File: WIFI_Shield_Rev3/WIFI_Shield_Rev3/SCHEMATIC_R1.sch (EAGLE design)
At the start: 32 parts, among them M1 NUCLEO-L452RE, U1 APDS-9306-065, U5 ESP32-C3-WROOM-02-N4

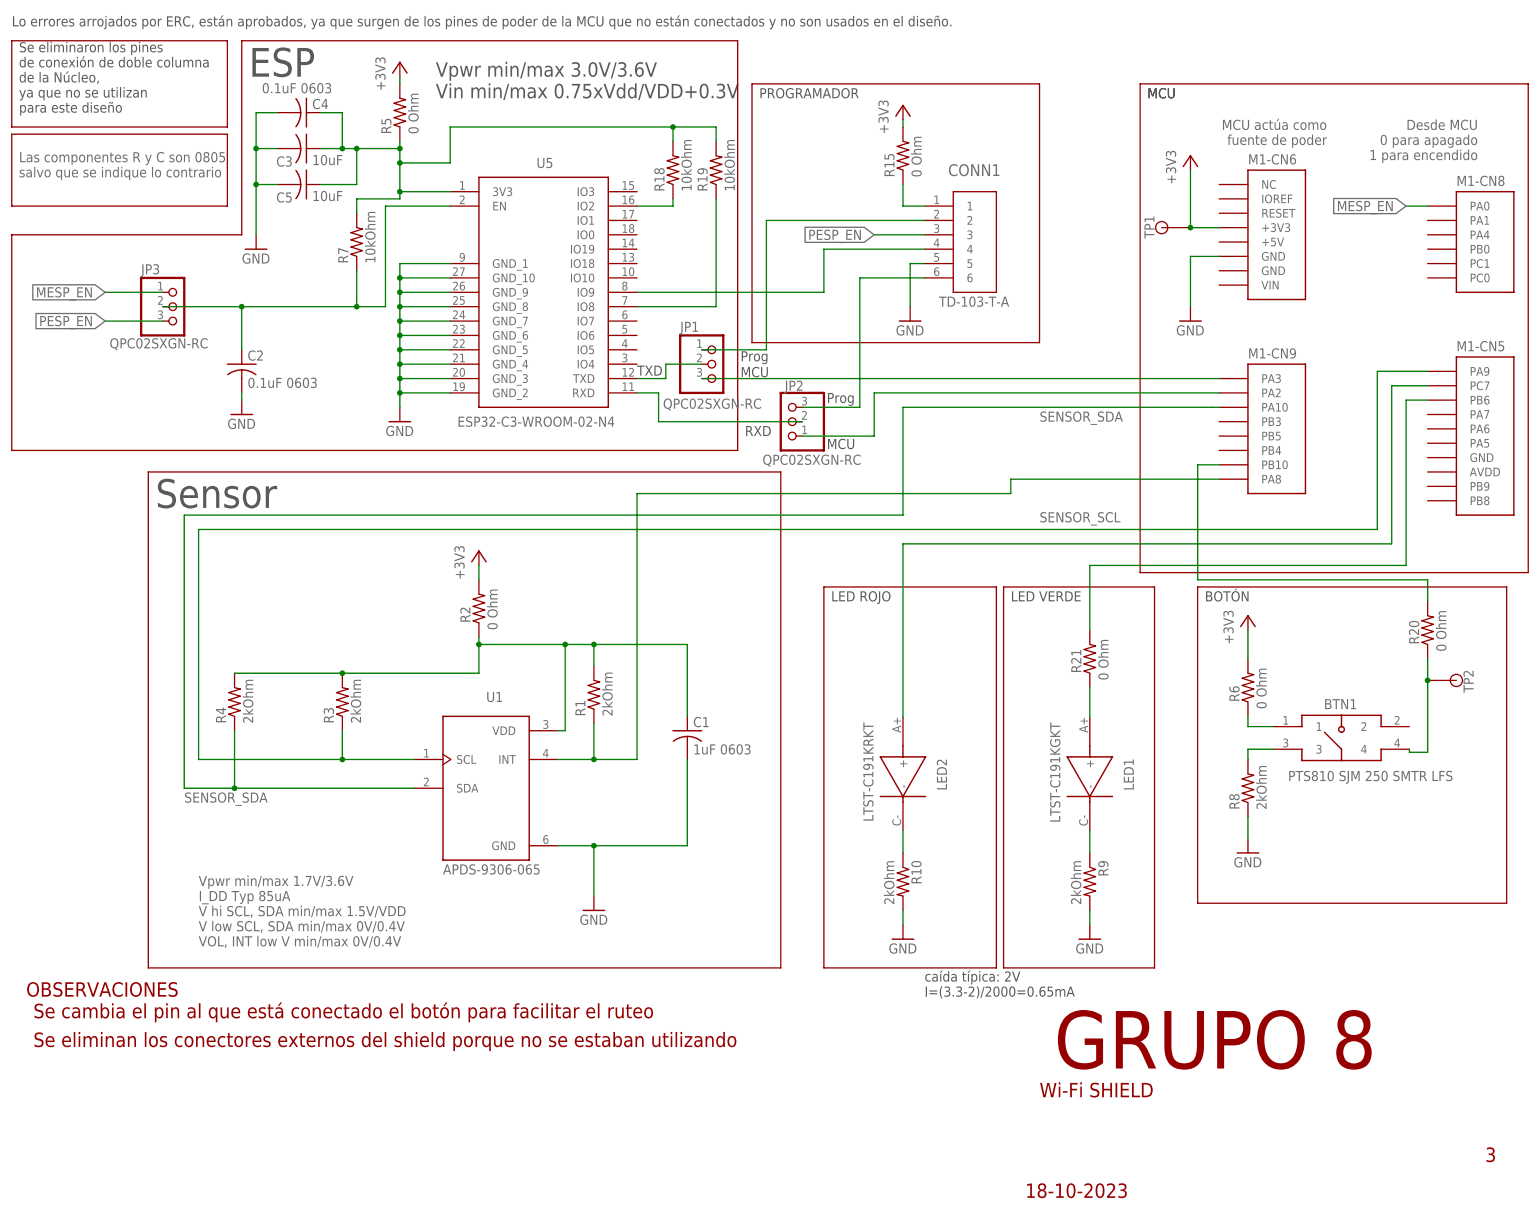
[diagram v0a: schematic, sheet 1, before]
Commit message: Arreglados los jumpers que no aparecían en el BOM. Agregados comentarios adicionales
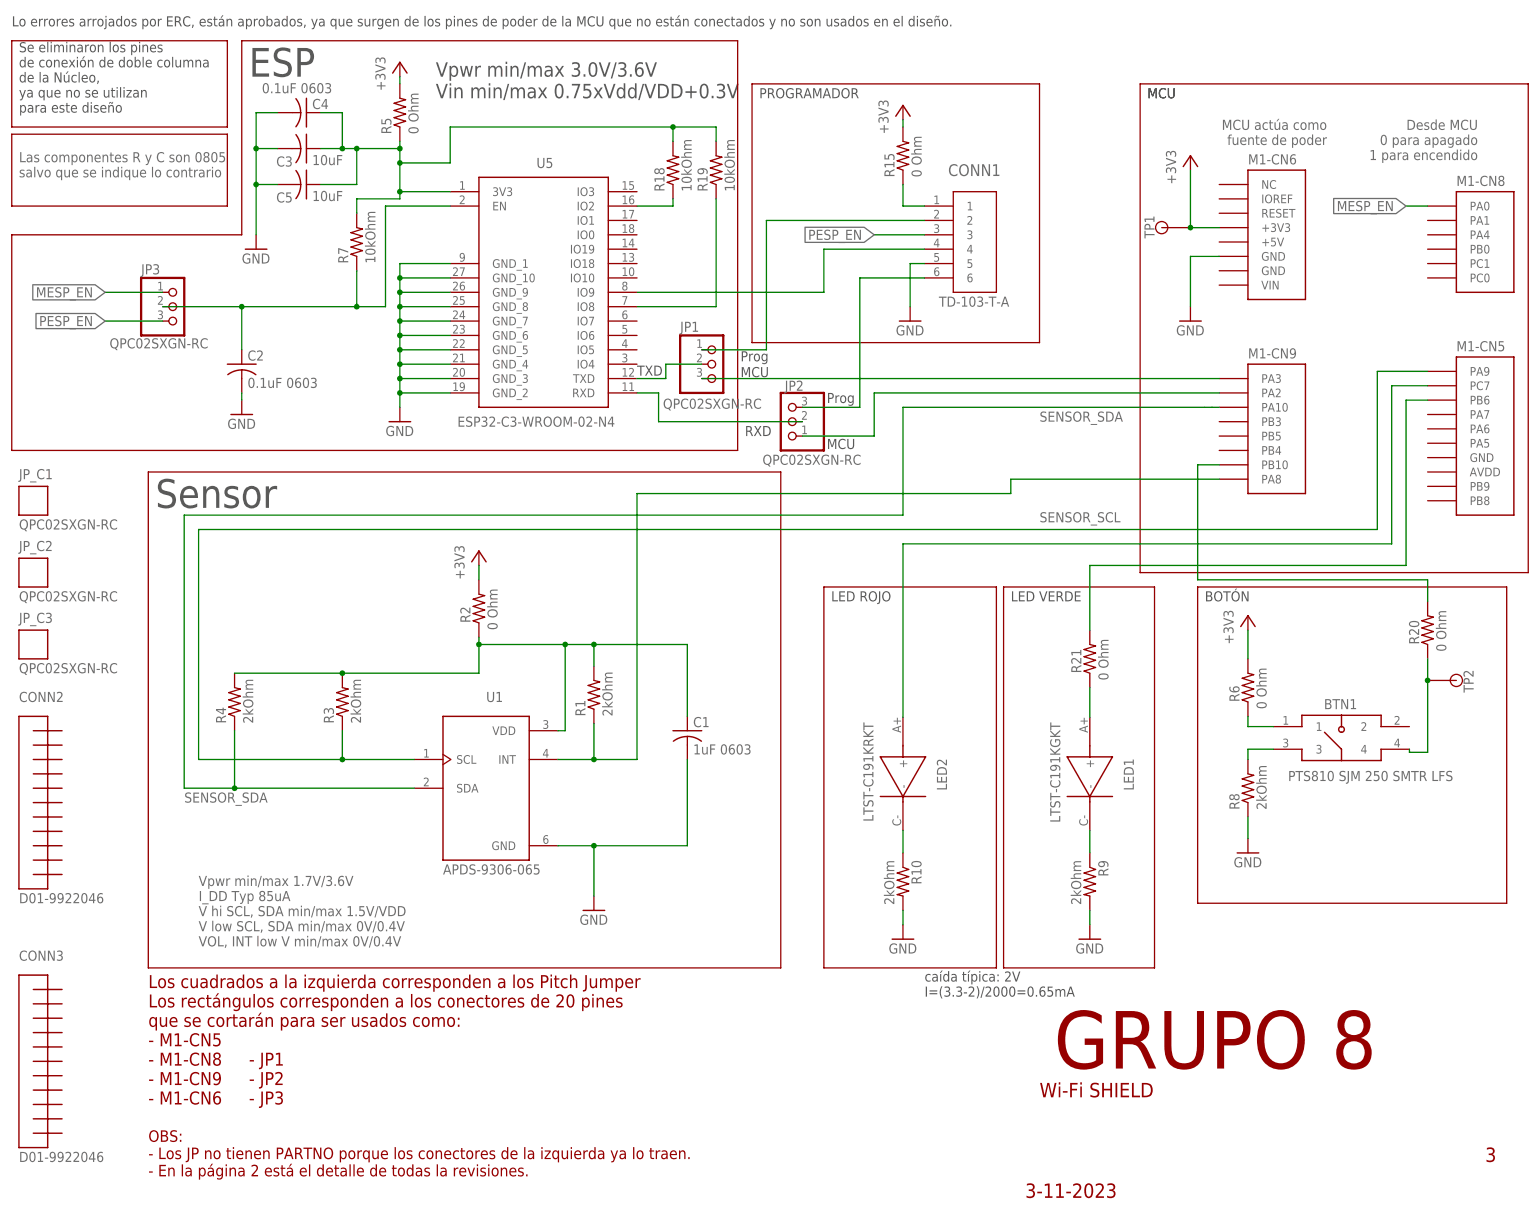
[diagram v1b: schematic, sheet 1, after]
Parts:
- added JP_C1, JP_C2, JP_C3: QPC02SXGN-RC, QPC02SXGN-RC:QPC02SXGN-RC
- JP1, JP2, JP3: PARTNO QPC02SXGN-RC -> (none)
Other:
- note added: "- JP1 - JP2 - JP3"
- note added: "3-11-2023"
- note added: "Historial de revisiones Rev1: Revisión inicial Rev2: Se ajustaron un par de pines para facilitar el ruteo y se ajustó la librería de la NUCLEO para eliminar los pines sin usar. Se cambia el pin al que está conectado el botón para facilitar el ruteo Se eliminan los conectores externos del shield porque no se estaban utilizando Rev3: Cambiadas algunas resistencias de 0 Ohm por jumpers R11-R14, R16 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"
- note added: "Los cuadrados a la izquierda corresponden a los Pitch Jumper Los rectángulos corresponden a los conectores de 20 pines que se cortarán para ser usados como: - M1-CN5 - M1-CN8 - M1-CN9 - M1-CN6"
- note added: "OBS: - Los JP no tienen PARTNO porque los conectores de la izquierda ya lo traen. - En la página 2 está el detalle de todas la revisiones."
- note removed: "18-10-2023"
- note removed: "2-11-2023"
- note removed: "Historial de revisiones Rev1: Revisión inicial Rev2: Se ajustaron un par de pines para facilitar el ruteo y se ajustó la librería de la NUCLEO para eliminar los pines sin usar. Se cambia el pin al que está conectado el botón para facilitar el ruteo Se eliminan los conectores externos del shield porque no se estaban utilizando Rev3: Cambiadas algunas resistencias de 0 Ohm por jumpers"
- note removed: "OBSERVACIONES"
- note removed: "Se cambia el pin al que está conectado el botón para facilitar el ruteo"
- note removed: "Se eliminan los conectores externos del shield porque no se estaban utilizando"
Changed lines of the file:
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@@
 <setting verticaltext="up"/>
 </settings>
-<grid distance="0.01" unitdist="inch" unit="inch" style="lines" multiple="1" display="no" altdistance="0.01" altunitdist="inch" altunit="inch"/>
+<grid distance="0.05" unitdist="inch" unit="inch" style="lines" multiple="1" display="no" altdistance="0.01" altunitdist="inch" altunit="inch"/>
 <layers>
 <layer number="1" name="Top" color="4" fill="1" visible="no" active="no"/>
@@
 <attribute name="PARTNO" value="NUCLEO-L452RE"/>
 </part>
-<part name="JP1" library="pinhead edit" deviceset="PINHD-1X3" device="" package3d_urn="urn:adsk.eagle:package:22458/2" value="QPC02SXGN-RC">
+<part name="JP1" library="pinhead edit" deviceset="PINHD-1X3" device="" package3d_urn="urn:adsk.eagle:package:22458/2" value="QPC02SXGN-RC"/>
+<part name="JP2" library="pinhead edit" deviceset="PINHD-1X3" device="" package3d_urn="urn:adsk.eagle:package:22458/2" value="QPC02SXGN-RC"/>
+<part name="JP3" library="pinhead edit" deviceset="PINHD-1X3" device="" package3d_urn="urn:adsk.eagle:package:22458/2" value="QPC02SXGN-RC"/>
+<part name="FRAME2" library="frames" library_urn="urn:adsk.eagle:library:229" deviceset="A4-35SC" device=""/>
+<part name="CONN2" library="D01-9922046" deviceset="D01-9922046" device="" value="D01-9922046">
+<attribute name="PARTNO" value="D01-9922046 "/>
+</part>
+<part name="CONN3" library="D01-9922046" deviceset="D01-9922046" device="" value="D01-9922046">
 <attribute name="PARTNO" value="QPC02SXGN-RC"/>
 </part>
-<part name="JP2" library="pinhead edit" deviceset="PINHD-1X3" device="" package3d_urn="urn:adsk.eagle:package:22458/2" value="QPC02SXGN-RC">
+<part name="JP_C1" library="QPC02SXGN-RC" deviceset="QPC02SXGN-RC" device="" value="QPC02SXGN-RC">
 <attribute name="PARTNO" value="QPC02SXGN-RC"/>
 </part>
-<part name="JP3" library="pinhead edit" deviceset="PINHD-1X3" device="" package3d_urn="urn:adsk.eagle:package:22458/2" value="QPC02SXGN-RC">
+<part name="JP_C2" library="QPC02SXGN-RC" deviceset="QPC02SXGN-RC" device="" value="QPC02SXGN-RC">
 <attribute name="PARTNO" value="QPC02SXGN-RC"/>
 </part>
-<part name="FRAME2" library="frames" library_urn="urn:adsk.eagle:library:229" deviceset="A4-35SC" device=""/>
+<part name="JP_C3" library="QPC02SXGN-RC" deviceset="QPC02SXGN-RC" device="" value="QPC02SXGN-RC">
+<attribute name="PARTNO" value="QPC02SXGN-RC"/>
+</part>
 </parts>
 <sheets>
@@
 <text x="35.56" y="-67.31" size="2.54" layer="94">Wi-Fi SHIELD</text>
 <text x="114.3" y="-78.74" size="2.54" layer="94">3</text>
-<text x="33.02" y="-85.09" size="2.54" layer="94">18-10-2023</text>
+<text x="33.02" y="-85.09" size="2.54" layer="94">3-11-2023</text>
 <text x="38.1" y="-62.23" size="10.16" layer="94">GRUPO 8</text>
-<text x="-142.24" y="-53.34" size="2.54" layer="94">Se cambia el pin al que está conectado el botón para facilitar el ruteo</text>
-<text x="-143.51" y="-49.53" size="2.54" layer="94">OBSERVACIONES</text>
-<text x="-142.24" y="-58.42" size="2.54" layer="94">Se eliminan los conectores externos del shield porque no se estaban utilizando</text>
 <text x="-16.51" y="49.53" size="1.778" layer="97">RXD</text>
 <text x="-2.032" y="55.372" size="1.778" layer="97">Prog</text>
@@
 <text x="-17.272" y="59.944" size="1.778" layer="97">MCU</text>
 <text x="-17.272" y="62.738" size="1.778" layer="97">Prog</text>
+<text x="-121.92" y="-68.58" size="2.286" layer="94">Los cuadrados a la izquierda corresponden a los Pitch Jumper
+Los rectángulos corresponden a los conectores de 20 pines
+que se cortarán para ser usados como:
+- M1-CN5
+- M1-CN8
+- M1-CN9
+- M1-CN6</text>
+<text x="-121.92" y="-81.28" size="2.032" layer="94">OBS:
+- Los JP no tienen PARTNO porque los conectores de la izquierda ya lo traen.
+- En la página 2 está el detalle de todas la revisiones.</text>
+<text x="-104.14" y="-68.58" size="2.286" layer="94">- JP1
+- JP2
+- JP3</text>
 </plain>
 <instances>
@@
 <attribute name="NAME" x="-27.94" y="67.945" size="1.778" layer="95"/>
 <attribute name="VALUE" x="-30.988" y="54.356" size="1.778" layer="96"/>
-<attribute name="PARTNO" x="-21.59" y="62.23" size="1.778" layer="96" display="off"/>
 </instance>
 <instance part="JP2" gate="A" x="-8.89" y="52.07" smashed="yes" rot="R180">
 <attribute name="NAME" x="-6.096" y="59.309" size="1.778" layer="95" rot="R180"/>
 <attribute name="VALUE" x="4.064" y="46.228" size="1.778" layer="96" rot="R180"/>
-<attribute name="PARTNO" x="-8.89" y="52.07" size="1.778" layer="96" rot="R180" display="off"/>
 </instance>
 <instance part="JP3" gate="A" x="-116.84" y="72.39" smashed="yes">
 <attribute name="NAME" x="-123.19" y="78.105" size="1.778" layer="95"/>
 <attribute name="VALUE" x="-128.778" y="65.024" size="1.778" layer="96"/>
-<attribute name="PARTNO" x="-116.84" y="72.39" size="1.778" layer="96" display="off"/>
+</instance>
+<instance part="CONN2" gate="G$1" x="-142.24" y="-15.24" smashed="yes">
+<attribute name="NAME" x="-144.78" y="2.54" size="1.778" layer="95"/>
+<attribute name="VALUE" x="-144.78" y="-33.02" size="1.778" layer="95"/>
+<attribute name="PARTNO" x="-142.24" y="-15.24" size="1.778" layer="96" display="off"/>
+</instance>
+<instance part="CONN3" gate="G$1" x="-142.24" y="-60.96" smashed="yes">
+<attribute name="NAME" x="-144.78" y="-43.18" size="1.778" layer="95"/>
+<attribute name="VALUE" x="-144.78" y="-78.74" size="1.778" layer="95"/>
+<attribute name="PARTNO" x="-142.24" y="-60.96" size="1.778" layer="96" display="off"/>
+</instance>
+<instance part="JP_C1" gate="G$1" x="-142.24" y="38.1" smashed="yes">
+<attribute name="NAME" x="-144.78" y="41.91" size="1.778" layer="95"/>
+<attribute name="VALUE" x="-144.78" y="33.02" size="1.778" layer="96"/>
+<attribute name="PARTNO" x="-142.24" y="38.1" size="1.778" layer="96" display="off"/>
+</instance>
+<instance part="JP_C2" gate="G$1" x="-142.24" y="25.4" smashed="yes">
+<attribute name="NAME" x="-144.78" y="29.21" size="1.778" layer="95"/>
+<attribute name="VALUE" x="-144.78" y="20.32" size="1.778" layer="96"/>
+<attribute name="PARTNO" x="-142.24" y="25.4" size="1.778" layer="96" display="off"/>
+</instance>
+<instance part="JP_C3" gate="G$1" x="-142.24" y="12.7" smashed="yes">
+<attribute name="NAME" x="-144.78" y="16.51" size="1.778" layer="95"/>
+<attribute name="VALUE" x="-144.78" y="7.62" size="1.778" layer="96"/>
+<attribute name="PARTNO" x="-142.24" y="12.7" size="1.778" layer="96" display="off"/>
 </instance>
 </instances>
@@
 <plain>
 <text x="78.232" y="258.826" size="2.54" layer="94">Wi-Fi SHIELD</text>
-<text x="128.016" y="261.112" size="1.778" layer="94">2-11-2023</text>
+<text x="128.016" y="261.112" size="1.778" layer="94">3-11-2023</text>
 <text x="166.878" y="262.128" size="3.81" layer="94" rot="R180">Historial de revisiones
 Rev1: Revisión inicial
@@
 utilizando
 Rev3: Cambiadas algunas resistencias de 0 Ohm por jumpers
-</text>
+R11-R14, R16 y R17 sustituidas por JP1-JP3</text>
 </plain>
 <instances>
